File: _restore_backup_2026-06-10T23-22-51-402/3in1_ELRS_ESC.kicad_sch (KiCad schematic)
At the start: 32 parts, among them J1 XT30, P1 SM08B-SRSS-TB(LF)(SN), U5 LMR51420YDDCR, U6 TLV76733DRVR, U7 INA186A3IDCKR

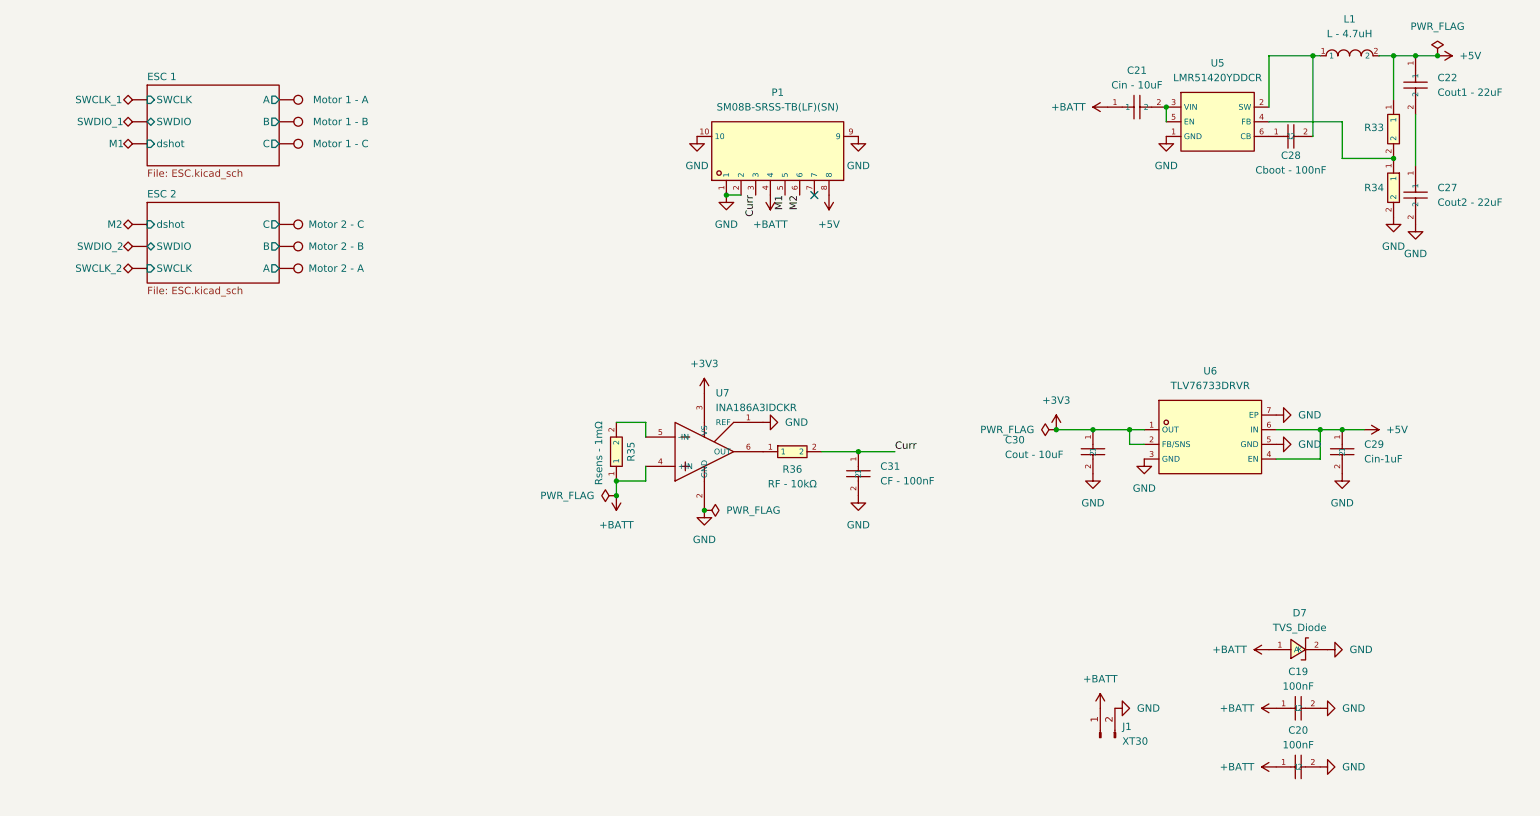
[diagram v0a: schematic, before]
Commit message: Schematic - Completed, PCB - Net Classes Assigned
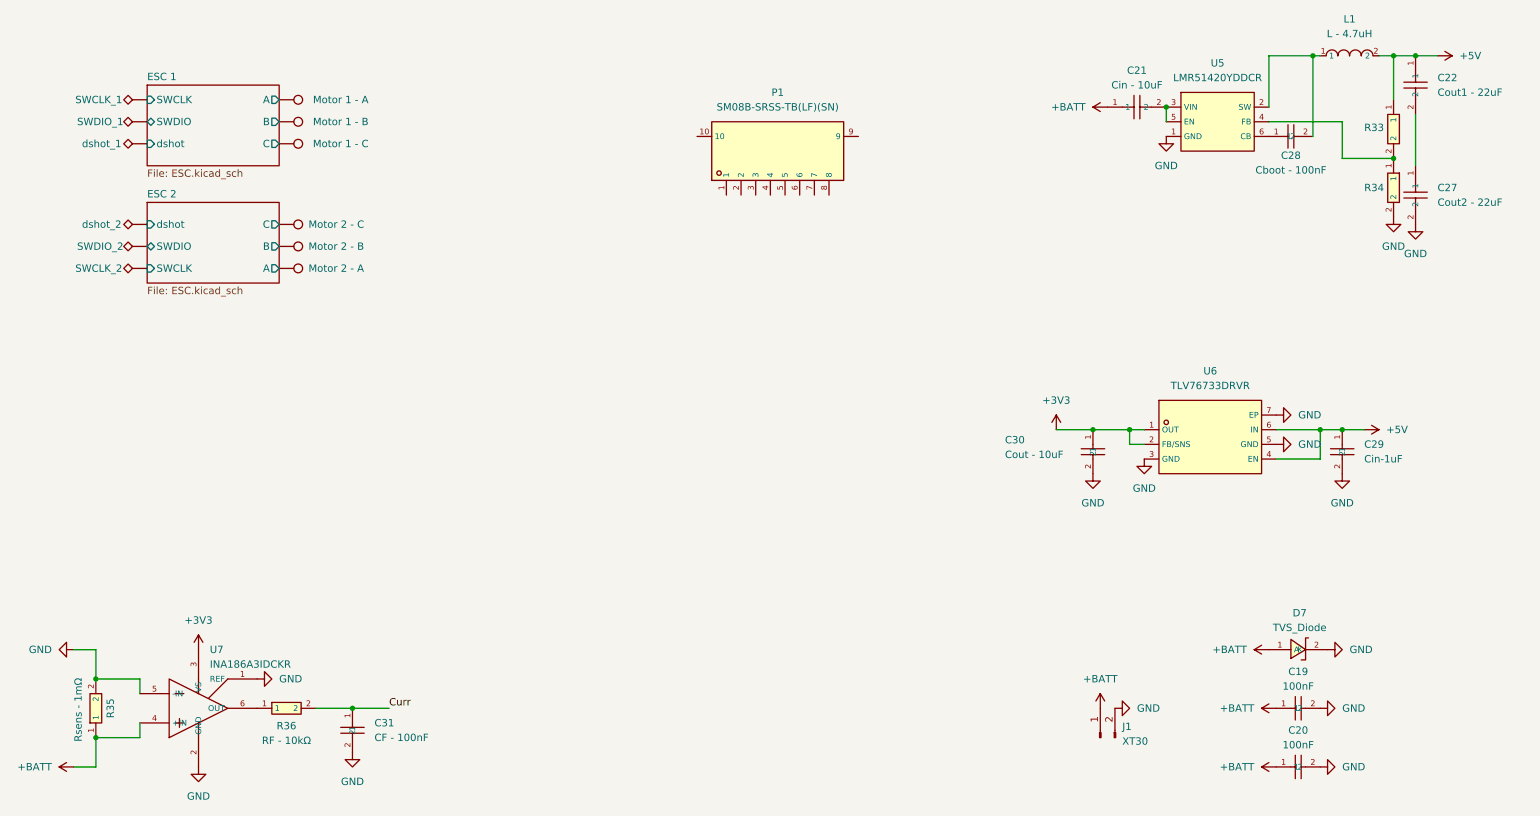
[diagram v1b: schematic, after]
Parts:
- renumbered M1 to dshot_1, M2 to dshot_2
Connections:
- net +5V: no longer P1.8
- net +BATT: no longer P1.4
- net Curr: no longer P1.3
- net GND: now also R35.2, U7.5 (-IN); no longer P1.1, P1.10, P1.2, P1.9
- net M1: no longer names the net of P1.5
- net M2: no longer names the net of P1.6
- no-connect marks 1 -> 0
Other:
- moved on the sheet: C31, R35, R36, U7
